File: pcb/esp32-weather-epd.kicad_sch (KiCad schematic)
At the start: 29 parts, among them J1 S2B-PH-K-S(LF)(SN), Q1 S8050, Q2 S8050, Q3 BRCS150P02ZJ, U1 CH340X, U2 TP4056X, U3 RT9080-33GJ5

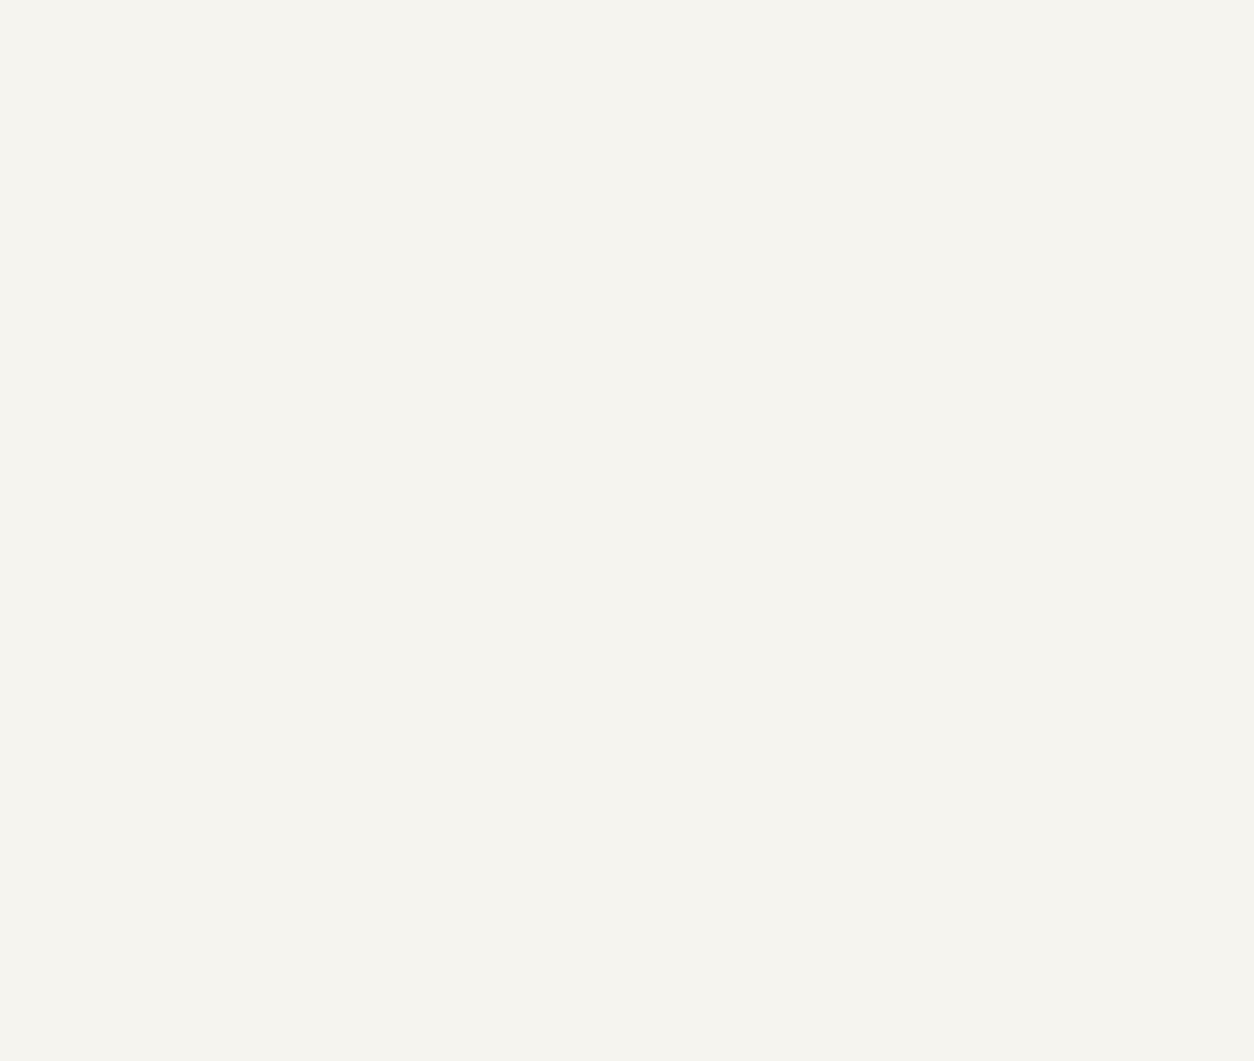
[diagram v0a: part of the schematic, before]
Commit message: add esp32 and peripheral circuit
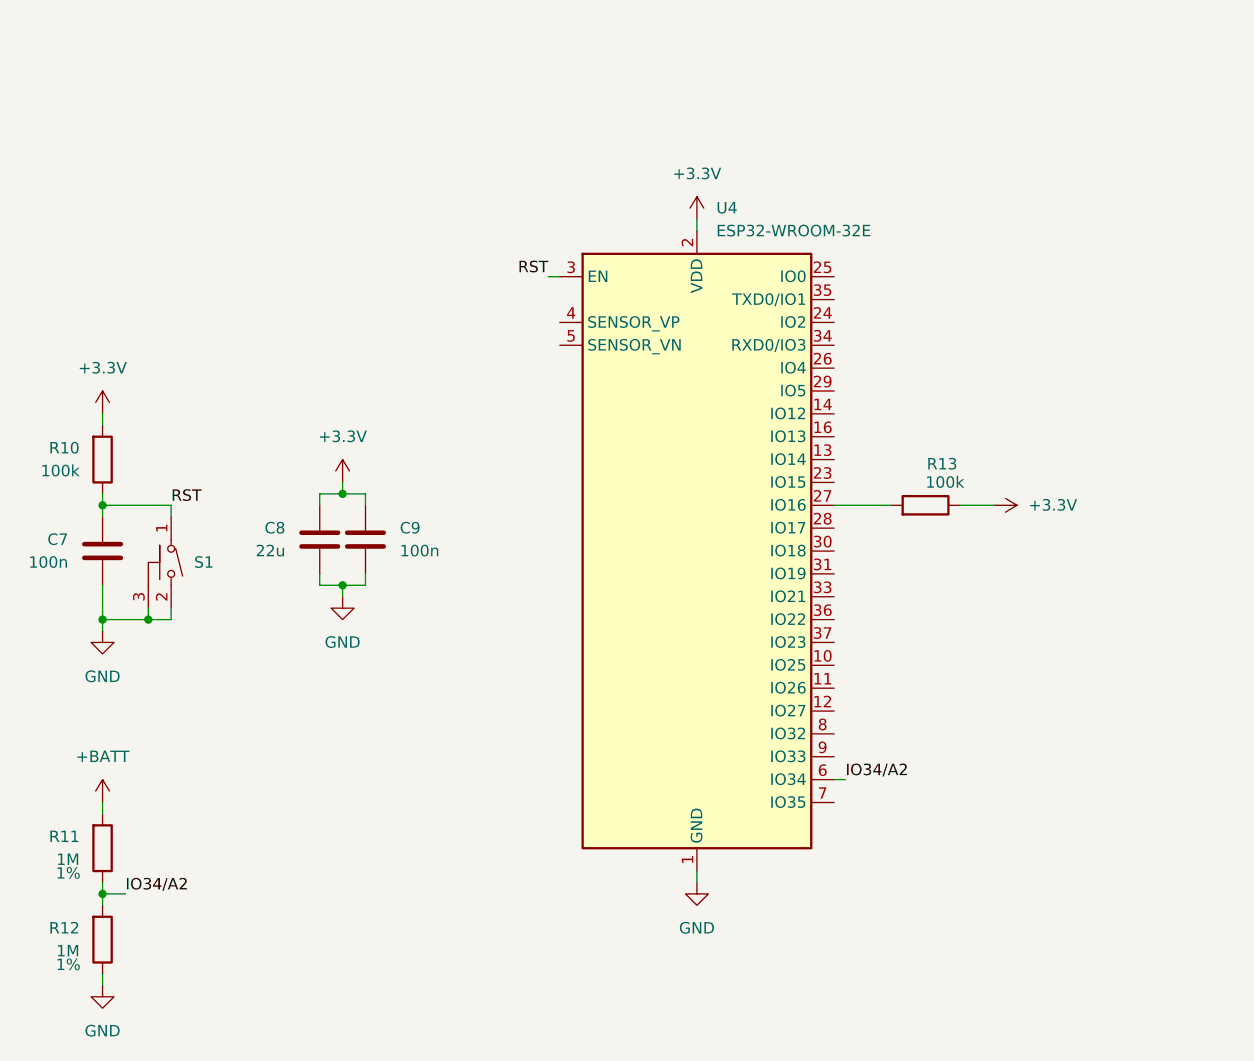
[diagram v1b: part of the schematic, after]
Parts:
- added C7, C9: 100n, symbol Device:C
- added C8: 22u, symbol Device:C
- added R10, R13: 100k, symbol Device:R
- added R11, R12: 1M, symbol Device:R
- added S1: YTS1C0033BBG01, libs:SW-SMD_YIYUAN_YTS1C003XXX, symbol 0_local_lib:YTS1C0033BBG01
- added U4: ESP32-WROOM-32E, RF_Module:ESP32-WROOM-32D, symbol RF_Module:ESP32-WROOM-32E
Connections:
- net +3.3V: now also C8.2, C9.2, R10.2, R13.1, U4.2 (VDD)
- net +BATT: now also R11.2
- net GND: now also C7.2, C8.1, C9.1, R12.1, S1.2, S1.3 (4), U4.1 (GND), U4.15 (GND), U4.38 (GND), U4.39 (GND)
- net RST: now also C7.1, R10.1, S1.1, U4.3 (EN)
- new net: R13.2, U4.27 (IO16)
- new net IO34/A2: R11.1, R12.2, U4.6 (IO34)

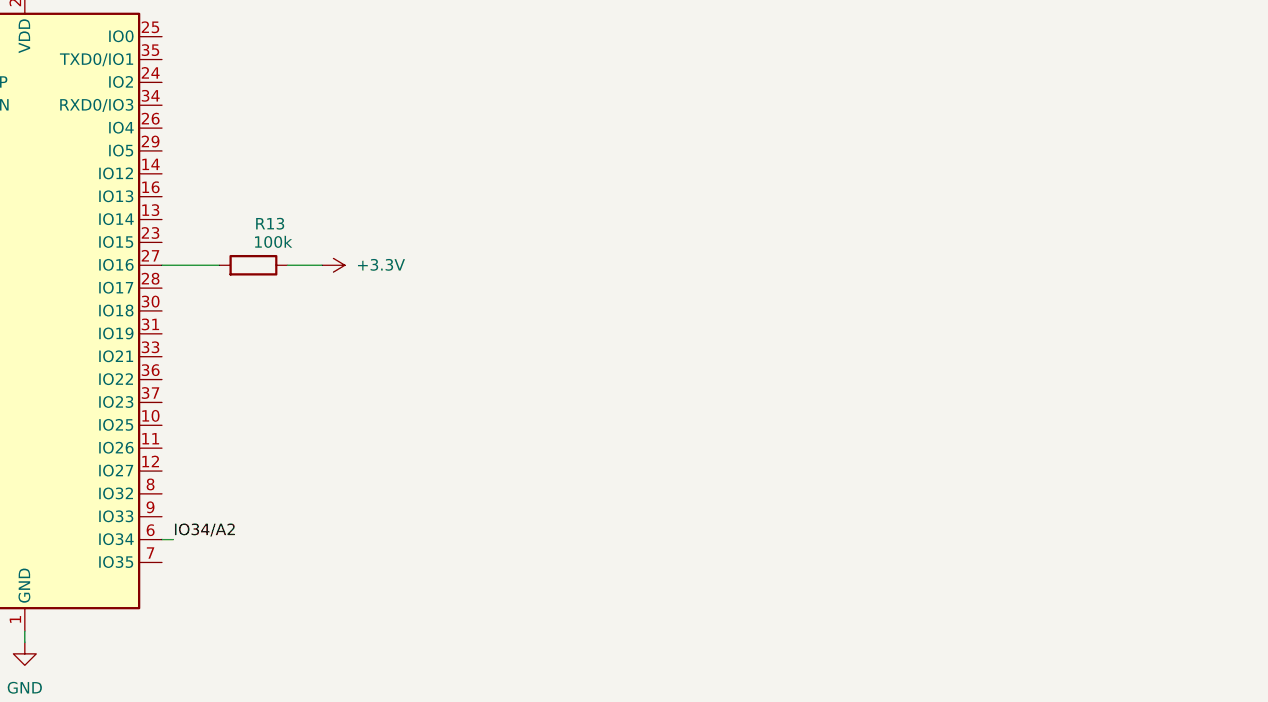
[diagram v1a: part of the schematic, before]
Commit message: add gas, pressure, temperature and humity sensor
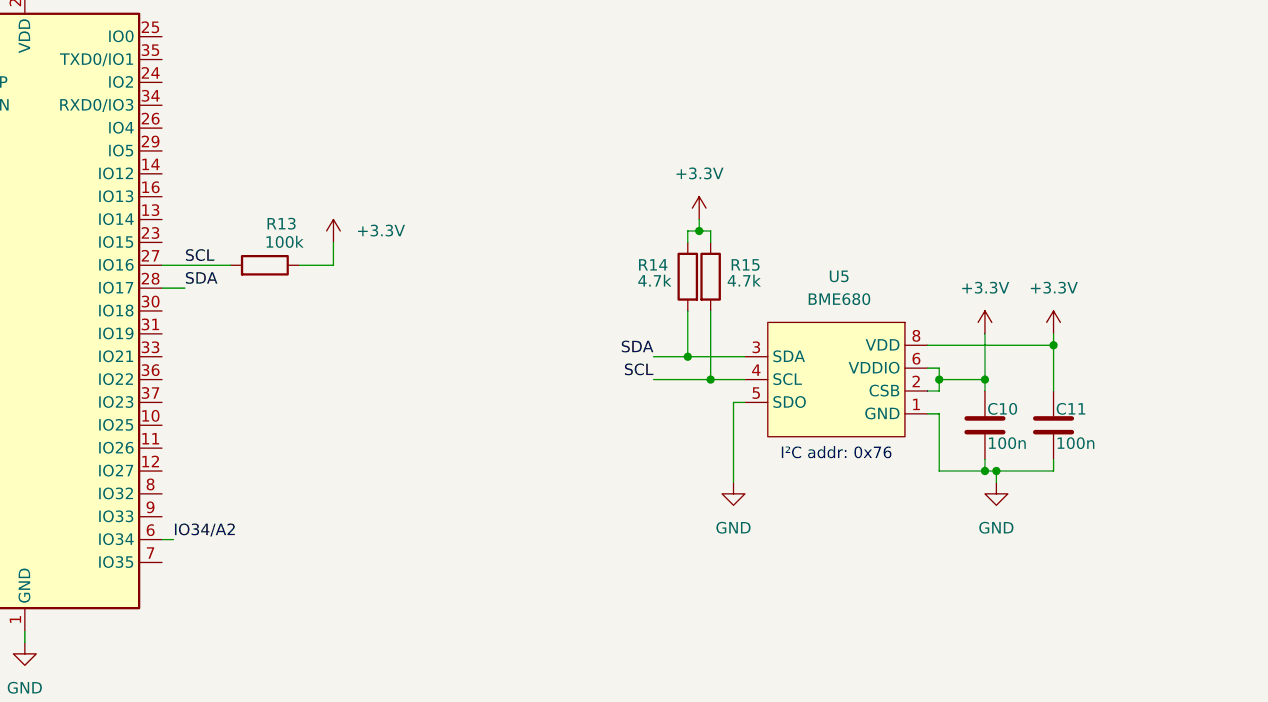
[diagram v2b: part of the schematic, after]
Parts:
- added C10, C11: 100n, symbol Device:C
- added R14, R15: 4.7k, symbol Device:R
- added U5: BME680, libs:LGA-8_L3.0-W3.0-P0.80-TR, symbol 0_local_lib:BME680
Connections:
- net +3.3V: now also C10.2, C11.2, R14.1, R15.1, U5.2 (CSB), U5.6 (VDDIO), U5.8 (VDD)
- net GND: now also C10.1, C11.1, U5.1 (GND), U5.5 (SDO)
- net SCL: now reaches R13.2, U4.27 (IO16)
- net SCL: now also R15.2, U5.4 (SCL)
- net SDA: now reaches U4.28 (IO17)
- net SDA: now also R14.2, U5.3 (SDA)
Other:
- note added: "I²C addr: 0x76"
- moved on the sheet: R13

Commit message: fix some lib link
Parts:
- S1: footprint libs:SW-SMD_YIYUAN_YTS1C003XXX -> 0_local_lib:SW-SMD_YIYUAN_YTS1C003XXX
- U5: footprint libs:LGA-8_L3.0-W3.0-P0.80-TR -> 0_local_lib:LGA-8_L3.0-W3.0-P0.80-TR
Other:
- moved on the sheet: C10, C11, R14, R15, U5

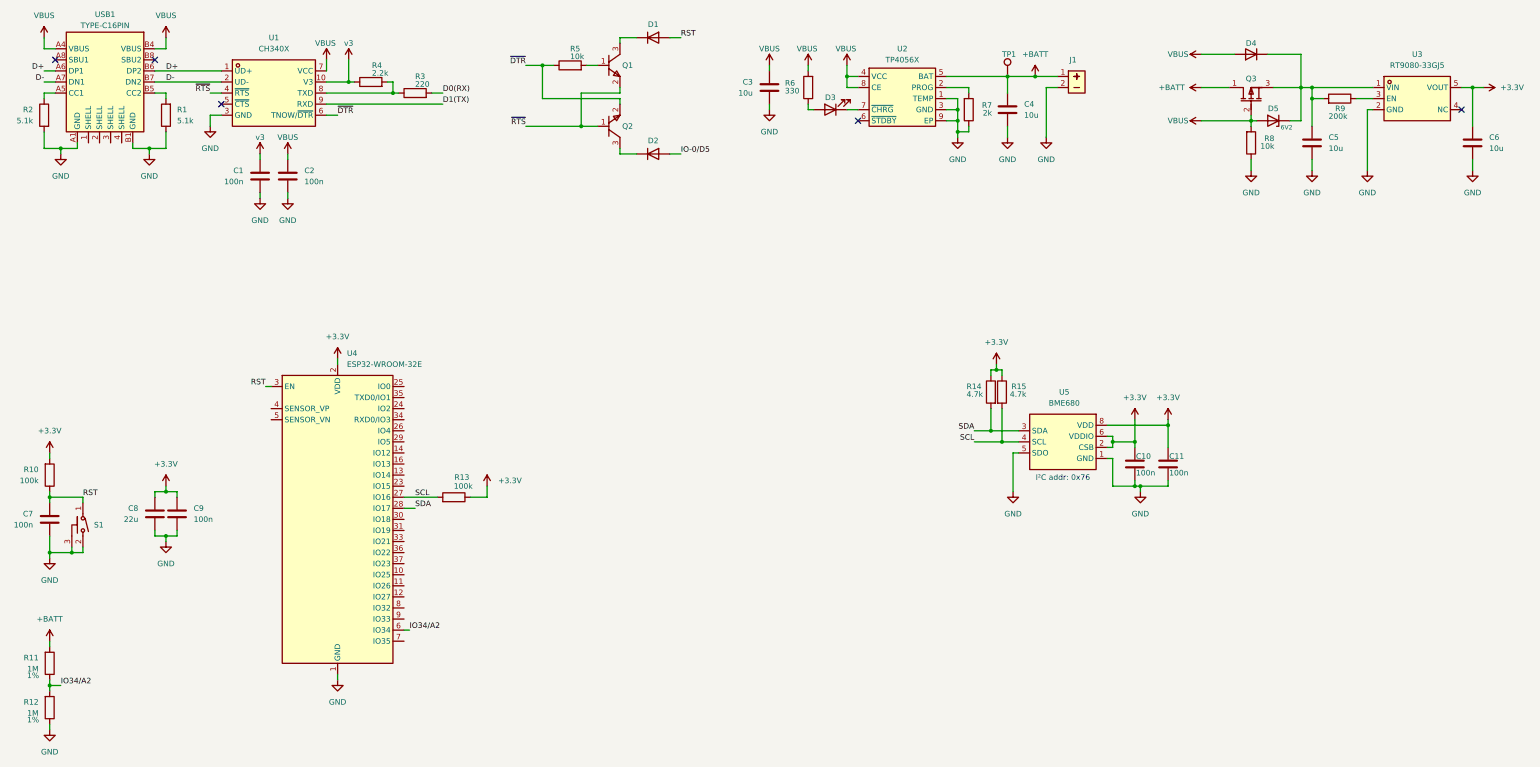
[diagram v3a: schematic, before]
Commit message: add epaper connector and needed circuitry
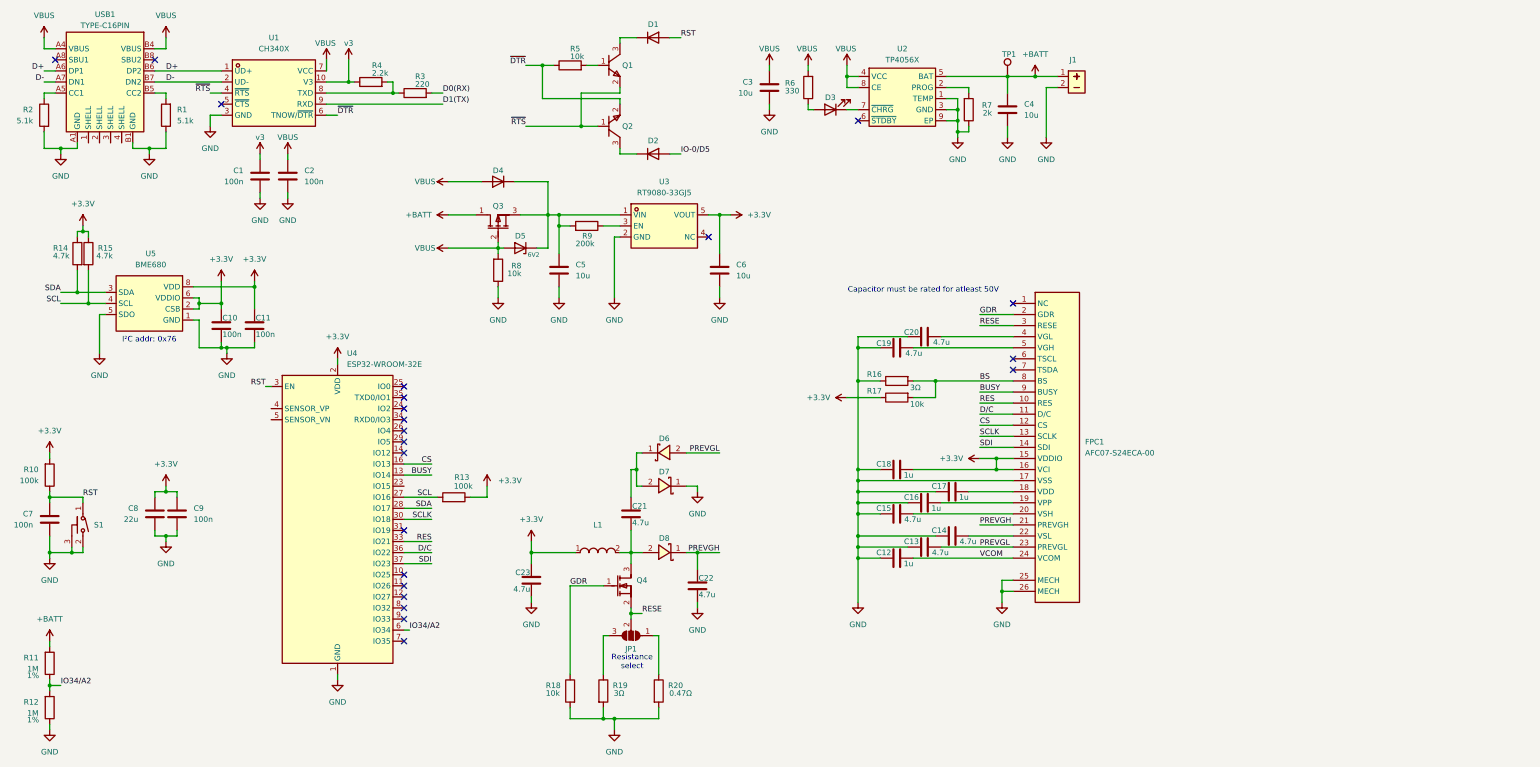
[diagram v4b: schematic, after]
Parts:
- added C12, C16, C17, C18: 1u, symbol Device:C
- added C13, C14, C15, C19, C20, C21, C22, C23: 4.7u, symbol Device:C
- added D6, D7, D8: MBR0530T1G, 0_local_lib:SOD-123_L2.7-W1.6-LS3.7-RD-1, symbol 0_local_lib:MBR0530T1G
- added FPC1: AFC07-S24ECA-00, 0_local_lib:FPC-SMD_AFC07-S24ECA-00, symbol 0_local_lib:AFC07-S24ECA-00
- added JP1: Resistanceselect, Jumper:SolderJumper-3_P1.3mm_Open_RoundedPad1.0x1.5mm_NumberLabels, symbol Jumper:SolderJumper_3_Open
- added L1: CKCSA3010-10UH/M, 0_local_lib:IND-SMD_L3.0-W3.0-1, symbol 0_local_lib:CKCSA3010-10UH_M
- added Q4: SI1308EDL-T1-GE3, 0_local_lib:SOT-323_L2.0-W1.3-P1.30-LS2.1-BR, symbol 0_local_lib:SI1308EDL-T1-GE3
- added R16, R19: 3Ω, symbol Device:R
- added R17, R18: 10k, symbol Device:R
- added R20: 0.47Ω, symbol Device:R
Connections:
- net +3.3V: now also C18.1, C23.2, FPC1.15 (VDDIO), FPC1.16 (VCI), L1.1, R17.1
- net GND: now also C12.2, C13.2, C14.2, C15.2, C16.2, C17.2, C18.2, C19.2, C20.2, C22.1, C23.1, D7.1 (C), FPC1.17 (VSS), FPC1.25 (MECH), FPC1.26 (MECH), R16.1, R18.2, R19.2, R20.2
- net BUSY: now reaches U4.13 (IO14)
- net BUSY: now also FPC1.9 (BUSY)
- net CS: now reaches U4.16 (IO13)
- net CS: now also FPC1.12 (CS)
- net SCLK: now reaches U4.30 (IO18)
- net SCLK: now also FPC1.13 (SCLK)
- net RES: now reaches U4.33 (IO21)
- net RES: now also FPC1.10 (RES)
- net D/C: now reaches U4.36 (IO22)
- net D/C: now also FPC1.11 (D/C)
- net SDI: now reaches U4.37 (IO23)
- net SDI: now also FPC1.14 (SDI)
- new net: C21.1, D8.2 (A), L1.2, Q4.3 (D)
- new net: C21.2, D6.1 (C), D7.2 (A)
- new net: C17.1, FPC1.18 (VDD)
- new net: C16.1, FPC1.19 (VPP)
- new net: C15.1, FPC1.20 (VSH)
- new net: C14.1, FPC1.22 (VSL)
- new net: C20.1, FPC1.4 (VGL)
- new net: C19.1, FPC1.5 (VGH)
- new net: JP1.3 (B), R19.1
- new net: JP1.1 (A), R20.1
- new net BS: FPC1.8 (BS), R16.2, R17.2
- new net GDR: FPC1.2 (GDR), Q4.1 (G), R18.1
- new net PREVGH: C22.2, D8.1 (C), FPC1.21 (PREVGH)
- new net PREVGL: C13.1, D6.2 (A), FPC1.23 (PREVGL)
- new net RESE: FPC1.3 (RESE), JP1.2 (C), Q4.2 (S)
- new net VCOM: C12.1, FPC1.24 (VCOM)
- no-connect marks 5 -> 22
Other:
- note added: "Capacitor must be rated for atleast 50V"
- note added: "Resistance select"
- moved on the sheet: C10, C11, C5, C6, D4, D5, Q3, R14, R15, R8, R9, U3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
